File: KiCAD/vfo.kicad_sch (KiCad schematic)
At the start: 13 parts, among them Q1 J310, U3 MC1496

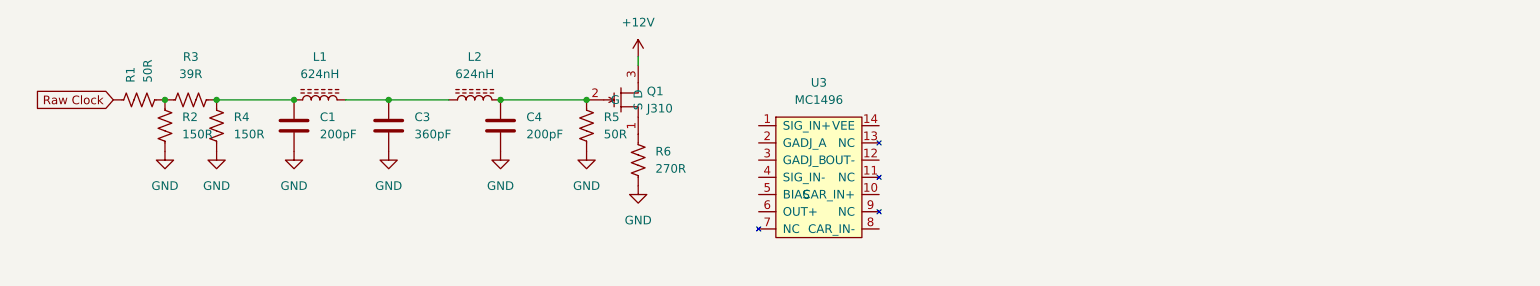
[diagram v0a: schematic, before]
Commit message: kicad vfo: Si5351 hookup + custom footprint + bulk footprint assign
vfo.kicad_sch — circuit changes (user-authored):
- Pi pad restored to current 62/240/62 Ω (was OLD 150/39/150)
- Added Si5351A breakout custom symbol (U1)
- Added 10 nF coupling cap (C_coup) + 0 Ω damping resistor (RS) between
  Si5351 CLK0 and pi pad — blocks the chip's 1.65 V DC offset that would
  otherwise overload the 8 mA output into RP1's 62 Ω shunt
- LPF inductors at the new T68-6 uniform 736 nH spec

vfo_input_stage.md — LPF cap retention clarified:
Caps stay at the original 220/390/390/220 (E12 silver mica) when using
T68-6 inductors. Documents the resulting filter shape change (cutoff
shifts 17.5 → 16.4 MHz, no longer strict Chebyshev) and the three
alternatives considered and rejected. Constructional uniformity over
filter spec.

xmitter.pretty/Adafruit_Si5351A_STEMMA.kicad_mod — new custom footprint:
Through-hole jumper-wire mount with 4 NPTH for M2.5 corner standoffs.
7 pads in a 1×7 column matching the symbol's pin names. No STEMMA QT
receptacle (SMT 1 mm pitch too small for hand-soldering with tremor).
Hole positions estimated from typical Adafruit board — verify with
calipers before fab.

fp-lib-table — registers the project-local xmitter footprint library.

vfo.kicad_sch — bulk footprint assignment:
- Resistors (R6, RP1, RP2, RP3, RS, RT1): R_Axial_DIN0207 P10.16mm
- NPO caps (CC1, C_coup): C_Disc_D5.0mm
- Silver mica 220 pF (CF1, CF7): C_Disc_D6.0mm
- Silver mica 390 pF (CF3, CF5): C_Disc_D7.5mm
- Toroids T68-6 (L2, L4, L6): L_Toroid_Horizontal_D14.0mm_P20.32mm
- Si5351 (U1): xmitter:Adafruit_Si5351A_STEMMA

Q1 (J310 TO-92) and U2 (MC1496 DIP-14) already had footprints; untouched.

Co-Authored-By: Claude Opus 4.7 <noreply@anthropic.com>
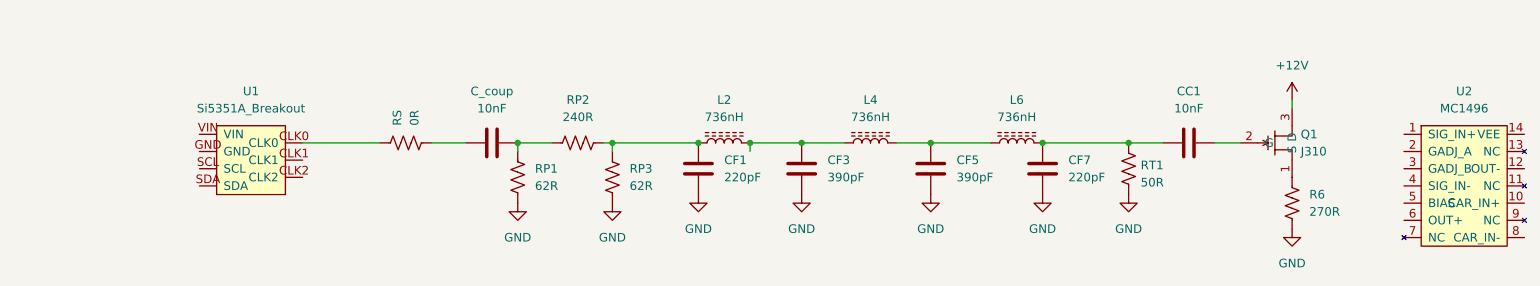
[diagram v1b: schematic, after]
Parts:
- removed R2, R4: 150R, symbol Device:R_US
- removed R3: 39R, symbol Device:R_US
- added CC1, C_coup: 10nF, Capacitor_THT:C_Disc_D5.0mm_W2.5mm_P5.00mm, symbol Device:C
- added CF3: 390pF, Capacitor_THT:C_Disc_D7.5mm_W2.5mm_P5.00mm, symbol Device:C
- added L4: 736nH, Inductor_THT:L_Toroid_Horizontal_D14.0mm_P20.32mm, symbol Device:L_Ferrite
- added RP1, RP3: 62R, Resistor_THT:R_Axial_DIN0207_L6.3mm_D2.5mm_P10.16mm_Horizontal, symbol Device:R_US
- added RP2: 240R, Resistor_THT:R_Axial_DIN0207_L6.3mm_D2.5mm_P10.16mm_Horizontal, symbol Device:R_US
- added U1: Si5351A_Breakout, xmitter:Adafruit_Si5351A_STEMMA, symbol xmitter:Si5351A_Breakout
- CF1: renamed from C1; value 200pF -> 220pF; footprint (none) -> Capacitor_THT:C_Disc_D6.0mm_W2.5mm_P5.00mm
- CF5: renamed from C3; value 360pF -> 390pF; footprint (none) -> Capacitor_THT:C_Disc_D7.5mm_W2.5mm_P5.00mm
- CF7: renamed from C4; value 200pF -> 220pF; footprint (none) -> Capacitor_THT:C_Disc_D6.0mm_W2.5mm_P5.00mm
- L2: renamed from L1; value 624nH -> 736nH; footprint (none) -> Inductor_THT:L_Toroid_Horizontal_D14.0mm_P20.32mm
- L6: renamed from L2; value 624nH -> 736nH; footprint (none) -> Inductor_THT:L_Toroid_Horizontal_D14.0mm_P20.32mm
- R6: footprint (none) -> Resistor_THT:R_Axial_DIN0207_L6.3mm_D2.5mm_P10.16mm_Horizontal
- RS: renamed from R1; value 50R -> 0R; footprint (none) -> Resistor_THT:R_Axial_DIN0207_L6.3mm_D2.5mm_P10.16mm_Horizontal
- RT1: renamed from R5; footprint (none) -> Resistor_THT:R_Axial_DIN0207_L6.3mm_D2.5mm_P10.16mm_Horizontal
- renumbered U3 to U2
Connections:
- net GND: now also CF3.2, RP1.2, RP3.2
- net at CF7.1, L6.2, RT1.1: now also CC1.1; no longer Q1.2 (G)
- net at CF5.1, L6.1: now also L4.2; no longer L2.2
- net at RS.2: now also C_coup.1
- net at CF1.1, L2.1: now also RP2.2, RP3.1
- net Raw Clock: no longer names the net of RS.1
- net Raw Clock: now also U1.CLK0
- new net: CC1.2, Q1.2 (G)
- new net: CF3.1, L2.2, L4.1
- new net: C_coup.2, RP1.1, RP2.1
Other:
- moved on the sheet: CF1, CF5, CF7, L2, L6, Q1, R6, RS, RT1, U2
